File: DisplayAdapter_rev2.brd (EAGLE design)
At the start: 21.8 x 21.1 mm, 2 parts

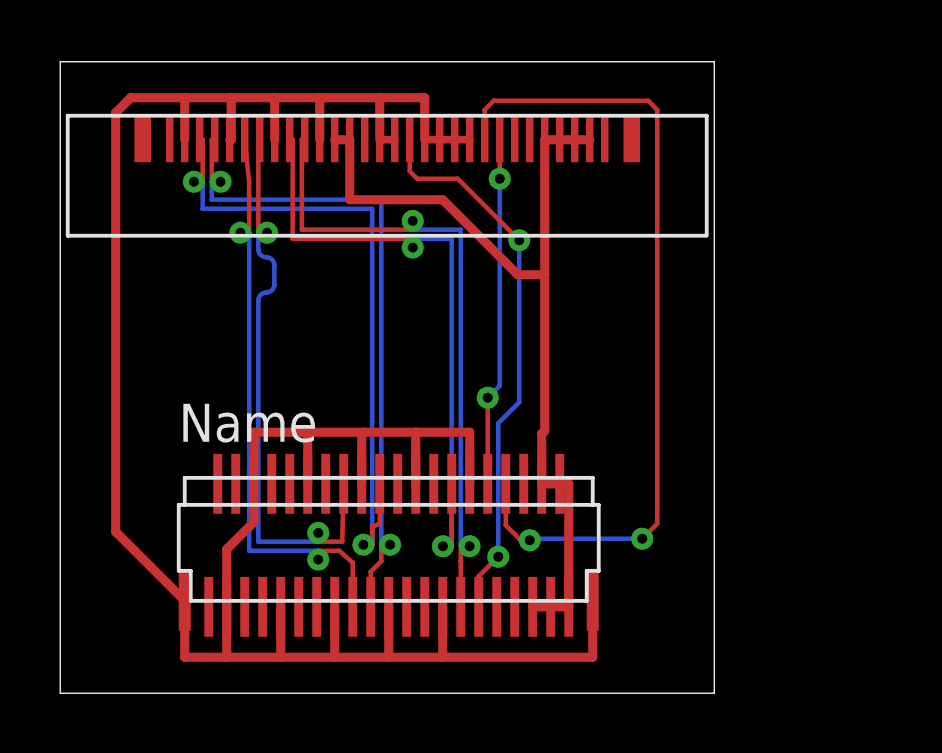
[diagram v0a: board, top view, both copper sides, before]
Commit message: added mounting holes
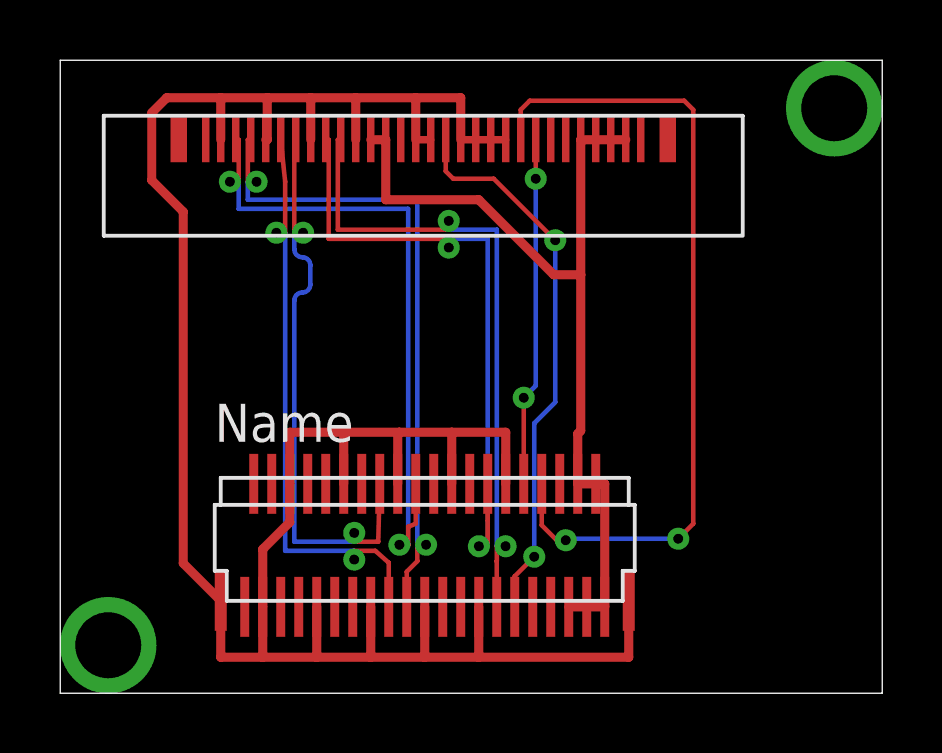
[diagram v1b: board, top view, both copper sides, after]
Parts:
- removed U$1: FH35C-41S-0.3SHW(50)_BAREBONE, FH35C_connector:FH35C-41S-0.3SHW(50)_BAREBONE
- added FH35C: FH35C-41S-0.3SHW(50)_BAREBONE, FH35C_connector:FH35C-41S-0.3SHW(50)_BAREBONE
- moved U$2 1.20 mm to (12.2, 17.2)
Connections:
- net AUX_CH_N: now also FH35C.PIN29; no longer U$1.PIN29
- net AUX_CH_P: now also FH35C.PIN28; no longer U$1.PIN28
- net LANE0_N: now also FH35C.PIN17; no longer U$1.PIN17
- net LANE0_P: now also FH35C.PIN16; no longer U$1.PIN16
- net LANE1_N: now also FH35C.PIN20; no longer U$1.PIN20
- net LANE1_P: now also FH35C.PIN19; no longer U$1.PIN19
- net N$10: now also FH35C.PIN12, FH35C.PIN15, FH35C.PIN18, FH35C.PIN21, FH35C.PIN24, FH35C.PIN27, FH35C.PIN3, FH35C.PIN30, FH35C.PIN42, FH35C.PIN43, FH35C.PIN6, FH35C.PIN9; no longer U$1.PIN12, U$1.PIN15, U$1.PIN18, U$1.PIN21, U$1.PIN24, U$1.PIN27, U$1.PIN3, U$1.PIN30, U$1.PIN42, U$1.PIN43, U$1.PIN6, U$1.PIN9
- net N$11: now also FH35C.PIN34; no longer U$1.PIN34
- net N$7: now also FH35C.PIN31; no longer U$1.PIN31
- net N$8: now also FH35C.PIN32; no longer U$1.PIN32
- net N$9: now also FH35C.PIN37, FH35C.PIN38, FH35C.PIN39, FH35C.PIN40, FH35C.PIN41; no longer U$1.PIN37, U$1.PIN38, U$1.PIN39, U$1.PIN40, U$1.PIN41
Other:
- board size 21.8 x 21.1 mm -> 27.4 x 21.1 mm
